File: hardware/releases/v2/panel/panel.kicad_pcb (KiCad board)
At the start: 4 copper layers, 98.5 x 76.5 mm, 129 parts, among them J1 KNX bus terminal pins, J2 AUX, J3 DALI, J4 Controller cable, J5 Interface DALI, J6 Interface logic, Q1 MJD45H11, Q2 BC857, U1 NCN5130MNTWG, U2 SCT2400TVBR, U3 REM3-2415S/A/CTRL 24V->15V 3W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, U4 TLP383, Y1 16MHz

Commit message: Regenerated V1 hardware release files with updated timestamps and mouse bite footprint reference consolidation
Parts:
- removed MB1, MB10, MB11, MB12, MB13, MB14, MB15, MB16, MB17, MB18, MB19, MB2, MB20, MB21, MB22, MB23, MB24, MB25, MB26, MB27, MB28, MB29, MB3, MB30, MB31, MB32, MB4, MB5, MB6, MB7, MB8, MB9: , 
- added MOUSE_BITES: DNP, , F.Cu at (0.00, 0.00)
- renumbered UI_C1 to C101, UI_C2 to C102, UI_C3 to C103, UI_C4 to C104, UI_C5 to C105, UI_C6 to C106, UI_C7 to C107, IF_C1 to C201, UI_D1 to D101, UI_D2 to D102, UI_D3 to D103, IF_D1 to D201, IF_D2 to D202, IF_D3 to D203, IF_D4 to D204, IF_D5 to D205, UI_J1 to J101, UI_J2 to J102, IF_J1 to J201, IF_J2 to J202, IF_Q1 to Q201, IF_Q2 to Q202, IF_Q3 to Q203, IF_Q4 to Q204, UI_R1 to R101, UI_R2 to R102, UI_R3 to R103, UI_R4 to R104, UI_R5 to R105, UI_R6 to R106, IF_R1 to R201, IF_R2 to R202, IF_R3 to R203, IF_R4 to R204, IF_R5 to R205, IF_R6 to R206, IF_R7 to R207, IF_R8 to R208, UI_SW1 to SW101, UI_SW2 to SW102, UI_U1 to U101, UI_U2 to U102, UI_U3 to U103, IF_U1 to U201, IF_U2 to U202
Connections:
- net IF_+3V3 renamed INTERFACE_+3V3
- net IF_DA1 renamed INTERFACE_DA1
- net IF_DA2 renamed INTERFACE_DA2
- net IF_DALI_BOOT renamed INTERFACE_DALI_BOOT
- net IF_DALI_GATE renamed INTERFACE_DALI_GATE
- net IF_DALI_GATE_SW renamed INTERFACE_DALI_GATE_SW
- net IF_DALI_RX renamed INTERFACE_DALI_RX
- net IF_DALI_SENSE renamed INTERFACE_DALI_SENSE
- net IF_DALI_TX renamed INTERFACE_DALI_TX
- net IF_DA_P renamed INTERFACE_DA_P
- net IF_GND renamed INTERFACE_GND
- net IF_GNDD renamed INTERFACE_GNDD
- net IF_N$1 renamed INTERFACE_N$1
- net IF_N$2 renamed INTERFACE_N$2
- net IF_N$3 renamed INTERFACE_N$3
- net IF_N$4 renamed INTERFACE_N$4
- net IF_RX_LIM_IN renamed INTERFACE_RX_LIM_IN

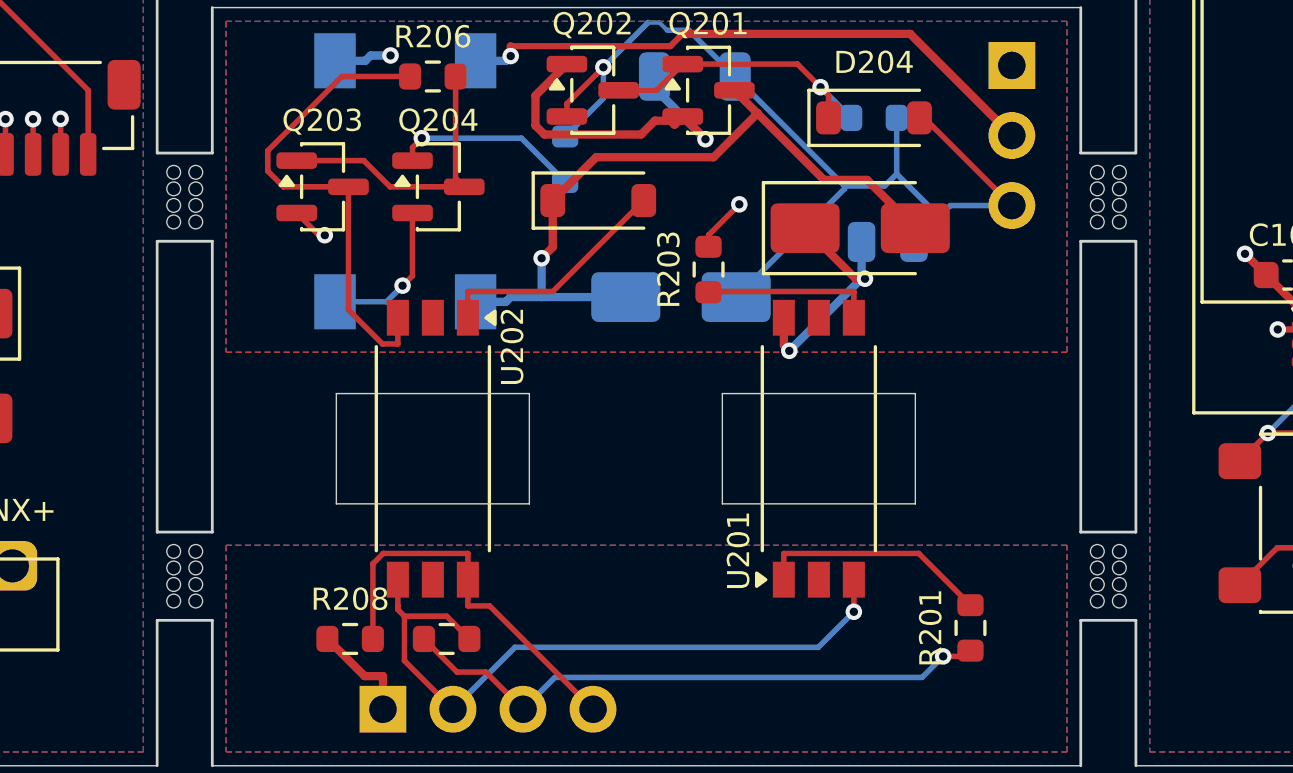
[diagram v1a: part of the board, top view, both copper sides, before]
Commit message: Added custom naming support for channels and groups with persistent storage, D4i power polling during commissioning, and updated web UI to display and edit names in lamp/group tiles and inspector panels
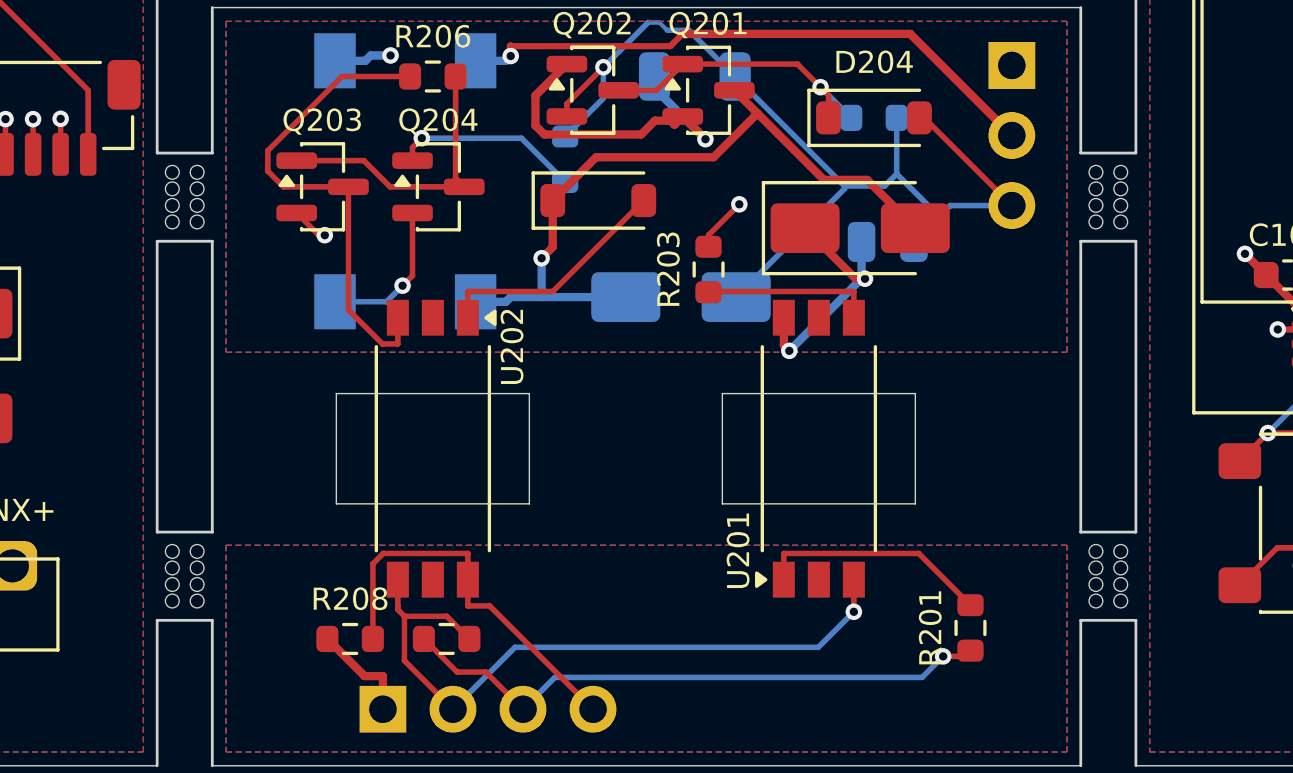
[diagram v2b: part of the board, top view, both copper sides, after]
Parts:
- removed MOUSE_BITES: DNP, 
- added MB1: DNP, , F.Cu at (32.0, -21.5)
- added MB10: DNP, , F.Cu at (33.0, -7.78)
- added MB11: DNP, , F.Cu at (32.0, -7.17)
- added MB12: DNP, , F.Cu at (33.0, -7.17)
- added MB13: DNP, , F.Cu at (32.0, -6.58)
- added MB14: DNP, , F.Cu at (33.0, -6.58)
- added MB15: DNP, , F.Cu at (32.0, -5.97)
- added MB16: DNP, , F.Cu at (33.0, -5.97)
- added MB17: DNP, , F.Cu at (65.5, -21.5)
- added MB18: DNP, , F.Cu at (66.5, -21.5)
- added MB19: DNP, , F.Cu at (65.5, -20.9)
- added MB2: DNP, , F.Cu at (33.0, -21.5)
- added MB20: DNP, , F.Cu at (66.5, -20.9)
- added MB21: DNP, , F.Cu at (65.5, -20.3)
- added MB22: DNP, , F.Cu at (66.5, -20.3)
- added MB23: DNP, , F.Cu at (65.5, -19.7)
- added MB24: DNP, , F.Cu at (66.5, -19.7)
- added MB25: DNP, , F.Cu at (65.5, -7.78)
- added MB26: DNP, , F.Cu at (66.5, -7.78)
- added MB27: DNP, , F.Cu at (65.5, -7.17)
- added MB28: DNP, , F.Cu at (66.5, -7.17)
- added MB29: DNP, , F.Cu at (65.5, -6.58)
- added MB3: DNP, , F.Cu at (32.0, -20.9)
- added MB30: DNP, , F.Cu at (66.5, -6.58)
- added MB31: DNP, , F.Cu at (65.5, -5.97)
- added MB32: DNP, , F.Cu at (66.5, -5.97)
- added MB4: DNP, , F.Cu at (33.0, -20.9)
- added MB5: DNP, , F.Cu at (32.0, -20.3)
- added MB6: DNP, , F.Cu at (33.0, -20.3)
- added MB7: DNP, , F.Cu at (32.0, -19.7)
- added MB8: DNP, , F.Cu at (33.0, -19.7)
- added MB9: DNP, , F.Cu at (32.0, -7.78)

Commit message: Updated DALI DC-DC converter from RECOM REM3-2415S/A to REC3-2415SRW/H2/A series across all variants, changed V3 OLED from 14-pin 0.5mm ZIF to 14-pin 0.62mm solder-tail FPC connector, and expanded assembly documentation with Mouser/Digi-Key/TME part numbers and alternative suppliers
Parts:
- U3: value REM3-2415S/A/CTRL 24V->15V 3W iso -> REC3-2415SRW/H2/A/CTRL 24V->15V 3W iso

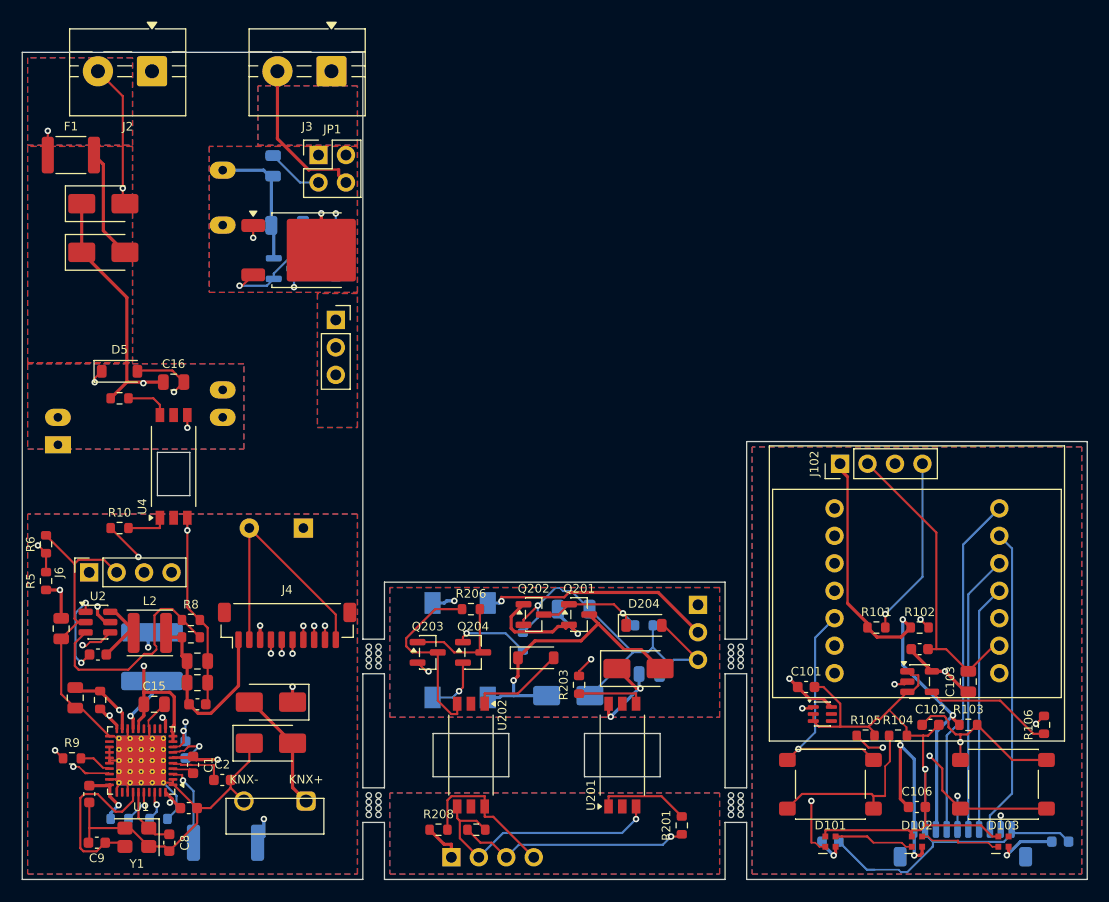
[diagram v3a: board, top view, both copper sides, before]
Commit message: Removed V1 hardware variant from CI workflows, updated AGENTS.md documentation to reflect V2/V3-only support
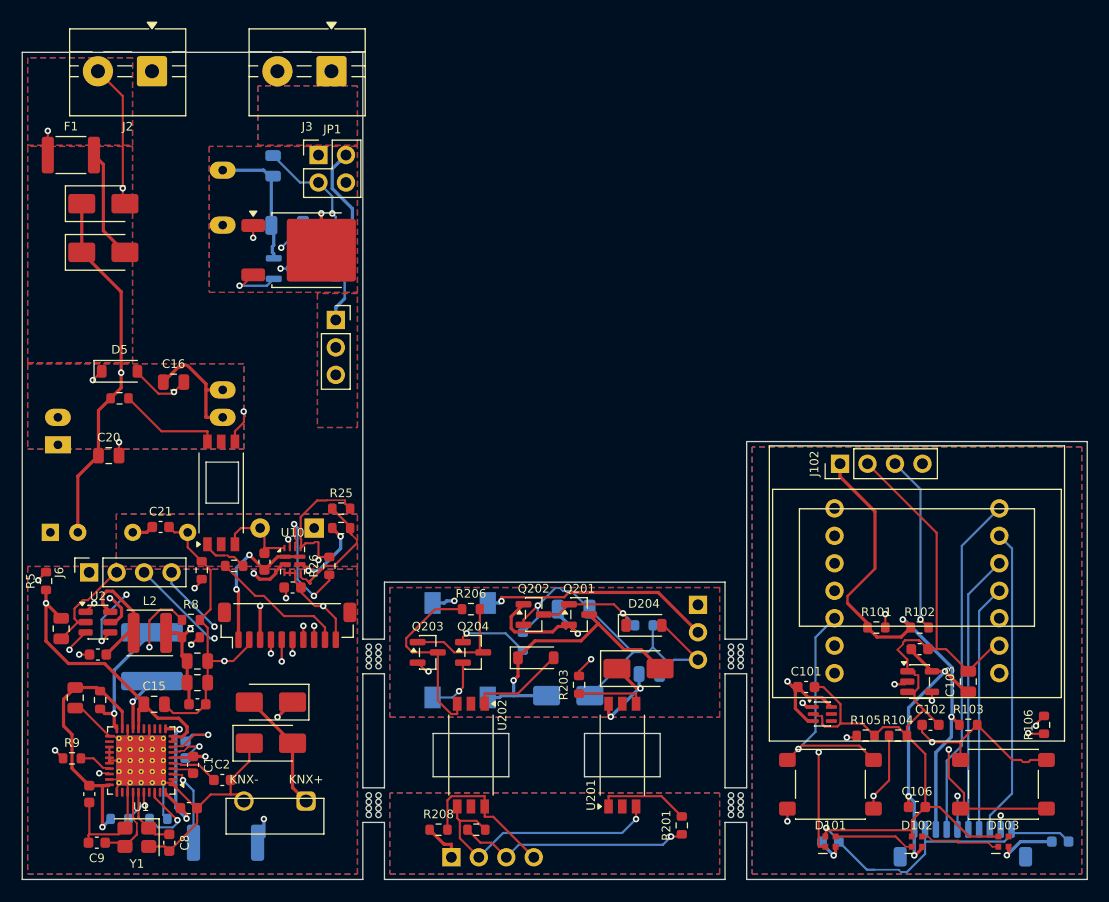
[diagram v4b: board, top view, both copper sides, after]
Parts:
- added C20: 10u 50V, Capacitor_SMD:C_0805_2012Metric, F.Cu at (8.00, -39.2)
- added C21: 10u 10V, Capacitor_SMD:C_0603_1608Metric, F.Cu at (12.8, -32.6)
- added C22: 100n 50V, Capacitor_SMD:C_0603_1608Metric, F.Cu at (25.0, -27.0)
- added C23: 10u 10V, Capacitor_SMD:C_0603_1608Metric, F.Cu at (22.4, -29.4)
- added R24: 30k, Resistor_SMD:R_0603_1608Metric, F.Cu at (29.5, -32.5)
- added R25: 10k, Resistor_SMD:R_0603_1608Metric, F.Cu at (29.5, -34.3)
- added R26: 100k 1%, Resistor_SMD:R_0603_1608Metric, F.Cu at (28.4, -29.0)
- added U10: TPS2121RUXR, Package_DFN_QFN:Texas_VQFN-HR-12_2x2.5mm_P0.5mm, F.Cu at (25.0, -29.5)
- added U9: TMR 1-2411 24V->5V 1W iso, gateway_fp:Converter_DCDC_TRACO_TMR1_SIP6, B.Cu at (2.60, -32.1)
- R203: value 22k -> 4k7
- R204: value 100k -> 10k
- R205: value 3R3 -> 2R
- R208: value 10k -> 4k7
- R5: value 120k 1% -> 100k 1%
- moved R6 14.6 mm to (16.6, -28.6)
- moved R10 11.2 mm to (19.6, -29.0)
- moved U4 5.04 mm to (18.4, -35.8)
- moved C4 1.00 mm to (27.0, -32.5)
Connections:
- C12 pad 1: +5V -> +5V_BUCK
- C13 pad 1: +5V -> +5V_BUCK
- C14 pad 1: +5V -> +5V_BUCK
- L2 pad 2: +5V -> +5V_BUCK
- R7 pad 1: +5V -> +5V_BUCK
- U101 pad 3: UI_GND -> UI_+5V_XIAO
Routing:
- net +5V_AUX: track 0.00 -> 30.3 mm, vias 0 -> 2
- net GND: track 158.7 -> 180.3 mm, vias 1 -> 3
- net GNDA: track 50.2 -> 71.5 mm, vias 2 -> 3
- net +5V_BUCK: track 0.00 -> 21.2 mm, vias 0 -> 2
- net AUX_P: track 35.5 -> 55.1 mm
- net VFILT: track 57.4 -> 74.0 mm, vias 3 -> 2
- net UI_GND: track 128.7 -> 116.0 mm
- net DALI_SUPPLY_OFF: track 25.1 -> 12.7 mm, vias 2 -> 0
- net N$11: track 0.00 -> 12.3 mm, vias 0 -> 2
- net CORE_PR1: track 0.00 -> 11.7 mm
- net +3V3_TRX: track 35.0 -> 46.1 mm, vias 4 -> 3
- net KNX_TXD: track 34.7 -> 24.0 mm
- net XTAL2: track 16.3 -> 7.58 mm
- net N$12: track 0.00 -> 7.44 mm, vias 0 -> 2
- net N$1: track 16.9 -> 23.3 mm, vias 2 -> 4
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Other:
- outline, holes or cut-outs redrawn

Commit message: Updated AUX-to-core converter from 1W TMR 1-2411 to 2W TMR 2411 (v3) and 3W TRN 3-2411 (v2) to handle WiFi TX peaks without KNX handover, relocated v3 converter to front protrusion tongue with AUX feed corridor along board edges, increased core hold-up capacitor C23 to 100µF 1206, added board slot between TRN3 pins 2/3 for creepage, updated domain regions and copper keepouts for new layouts, and added DCDC_SIP5/DCDC_SIP8_REMOTE symbols with converter parameter support in core_power.build()
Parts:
- C23: value 10u 10V -> 100u 6.3V; footprint Capacitor_SMD:C_0603_1608Metric -> Capacitor_SMD:C_1206_3216Metric
- U9: value TMR 1-2411 24V->5V 1W iso -> TRN 3-2411 24V->5V 3W iso; footprint gateway_fp:Converter_DCDC_TRACO_TMR1_SIP6 -> gateway_fp:Converter_DCDC_TRACO_TRN3_SIP5
- moved C23 8.02 mm to (15.0, -32.5)
- moved C21 3.68 mm to (9.40, -31.2)
- moved U9 1.50 mm to (2.60, -33.6)
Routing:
- net +5V: track 14.2 -> 27.0 mm, vias 2 -> 3
- net KNX_RXD: track 40.8 -> 28.0 mm
- net GNDA: track 71.5 -> 62.4 mm
- net +5V_BUCK: track 21.2 -> 28.1 mm
- net VDD1M: track 11.9 -> 17.3 mm, vias 1 -> 2
- net FANIN: track 6.77 -> 12.0 mm, vias 1 -> 2
- net N$3: track 22.6 -> 17.6 mm, vias 3 -> 0
- net AUX_P: track 55.1 -> 50.2 mm
- net VFILT: track 74.0 -> 78.5 mm, vias 2 -> 4
- net +3V3: track 23.9 -> 19.4 mm
- net DALI_RX: track 20.2 -> 16.5 mm, vias 2 -> 1
- net N$11: track 12.3 -> 15.4 mm
- net SW: track 10.9 -> 8.10 mm
- net KNX_TXD: track 24.0 -> 26.8 mm
- net CEQ2: track 6.09 -> 3.51 mm
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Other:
- outline, holes or cut-outs redrawn

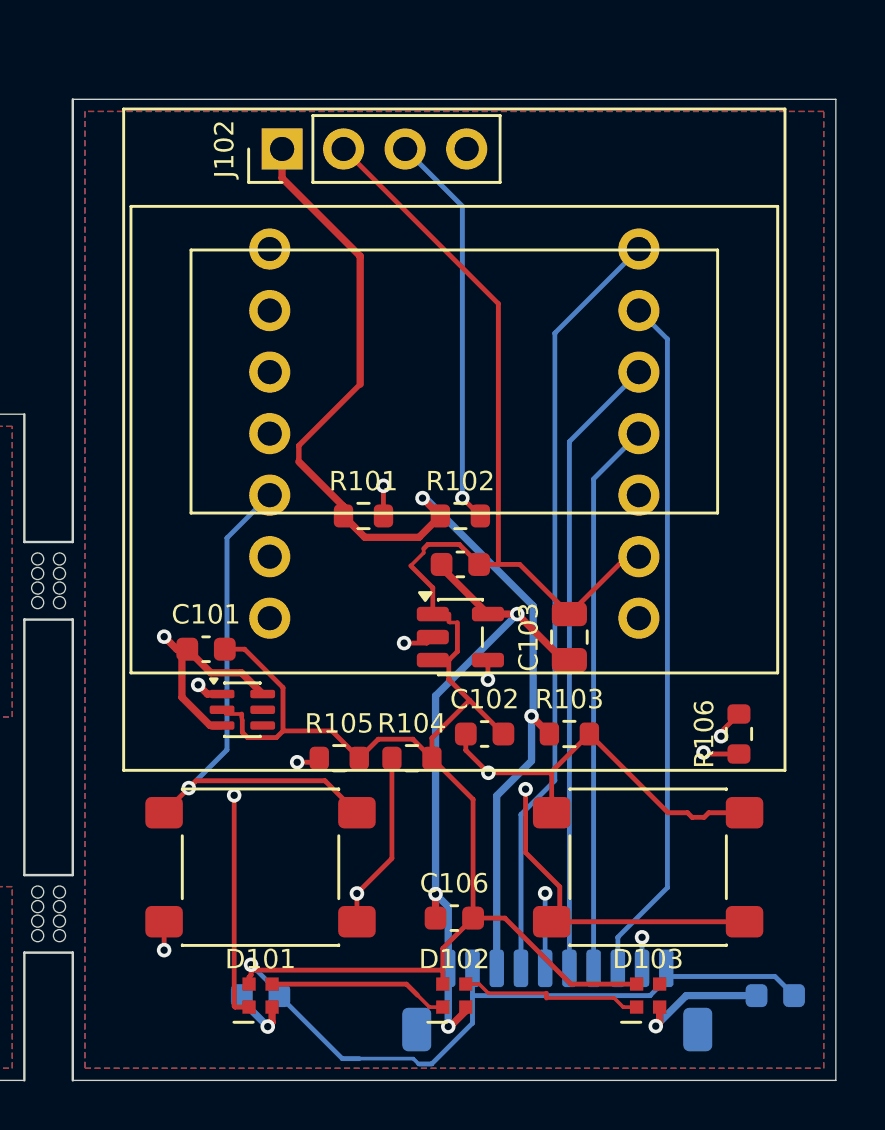
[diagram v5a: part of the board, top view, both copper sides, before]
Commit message: Unified V2/V3 UI buttons to Omron B3U-1000P with cover spring tabs
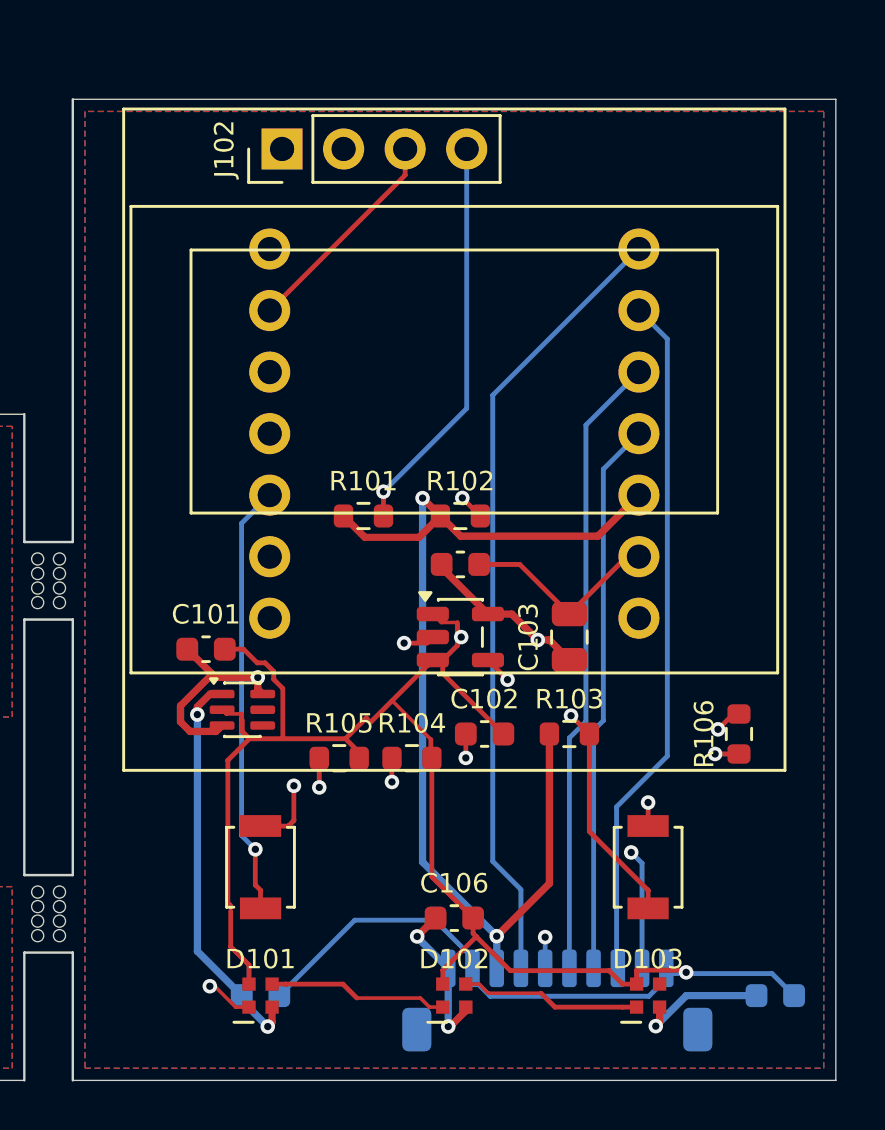
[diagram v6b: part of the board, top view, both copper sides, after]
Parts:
- SW101, SW102: footprint Button_Switch_SMD:SW_SPST_PTS645Sx43SMTR92 -> Button_Switch_SMD:SW_SPST_B3U-1000P
- turned SW101 to 90 degrees
- turned SW102 to 90 degrees
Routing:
- net UI_N$1: track 17.5 -> 8.32 mm
- net UI_N$2: track 25.0 -> 16.0 mm
- net UI_BTN_LADDER: track 51.6 -> 44.6 mm, vias 2 -> 3
- net UI_GND: track 116.0 -> 122.6 mm, vias 1 -> 2
- net UI_+3V3: track 56.6 -> 61.8 mm
- net UI_+5V_XIAO: track 29.8 -> 25.4 mm
- net UI_+5V: track 71.9 -> 68.2 mm
- net UI_I2C_SDA: track 20.5 -> 23.5 mm
- net UI_KNX_RXD: track 46.2 -> 43.5 mm
- net UI_I2C_SCL: track 25.4 -> 23.1 mm
- net UI_N$4: track 32.5 -> 30.5 mm
- net UI_DALI_SUPPLY_OFF: track 35.0 -> 36.4 mm
- net UI_KNX_TXD: track 31.7 -> 32.7 mm
